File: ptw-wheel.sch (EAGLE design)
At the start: 5 parts

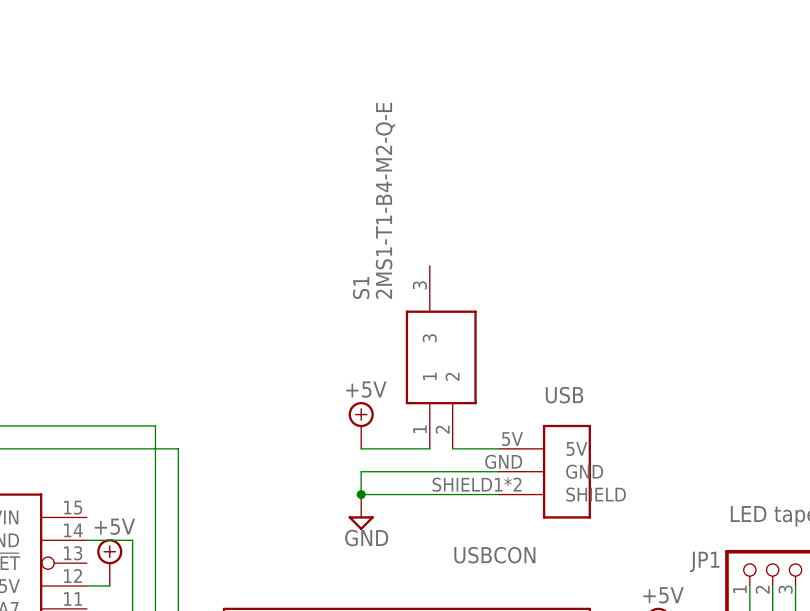
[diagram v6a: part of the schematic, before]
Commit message: - Replace toggle switch - Adjust positions
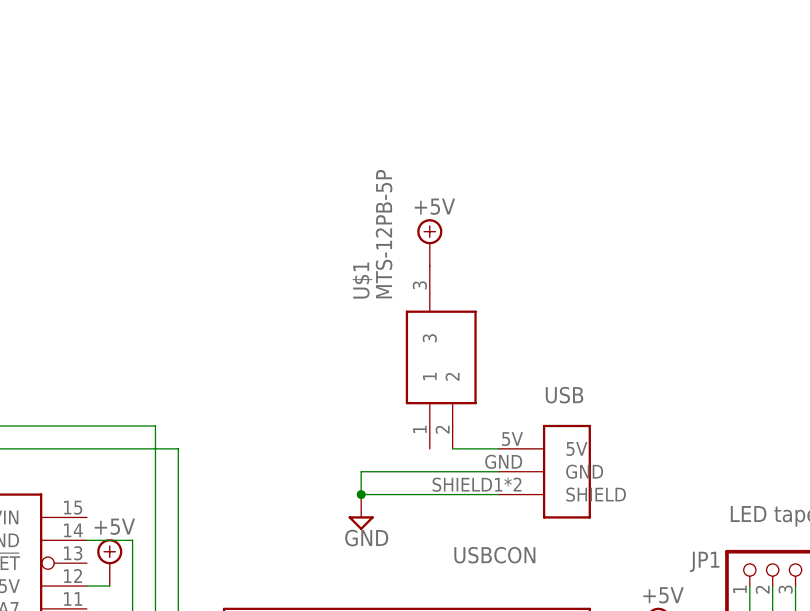
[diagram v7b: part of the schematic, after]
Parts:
- removed S1: 2MS1-T1-B4-M2-Q-E, 2MS1-T1-B4-VS2-Q-E:2MS1-T1-B4-M2-Q-E
- added U$1: MTS-12PB-5P, toggle-switch:MTS-12PB-5P
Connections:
- net +5V: now also U$1.3; no longer S1.1
- net N$1: now also U$1.2; no longer S1.2
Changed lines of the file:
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@@
 <part name="SUPPLY10" library="supply2" library_urn="urn:adsk.eagle:library:372" deviceset="GND" device=""/>
 <part name="KONASHI" library="konashiv2" deviceset="KONASHI2.0" device=""/>
-<part name="S1" library="2MS1-T1-B4-VS2-Q-E" deviceset="2MS1-T1-B4-M2-Q-E" device=""/>
+<part name="U$1" library="toggle-switch" deviceset="MTS-12PB-5P" device=""/>
 </parts>
 <sheets>
@@
 <attribute name="VALUE" x="51.435" y="34.925" size="1.778" layer="96"/>
 </instance>
-<instance part="SUPPLY6" gate="+5V" x="78.74" y="66.04" smashed="yes">
-<attribute name="VALUE" x="76.835" y="69.215" size="1.778" layer="96"/>
+<instance part="SUPPLY6" gate="+5V" x="86.36" y="86.36" smashed="yes">
+<attribute name="VALUE" x="84.455" y="89.535" size="1.778" layer="96"/>
 </instance>
 <instance part="SUPPLY9" gate="+5V" x="111.76" y="43.18" smashed="yes">
@@
 </instance>
 <instance part="KONASHI" gate="G$1" x="83.82" y="33.02" smashed="yes" rot="R90"/>
-<instance part="S1" gate="G$1" x="86.36" y="63.5" smashed="yes" rot="R90">
+<instance part="U$1" gate="G$1" x="86.36" y="63.5" smashed="yes" rot="R90">
 <attribute name="NAME" x="78.74" y="80.01" size="1.778" layer="95" rot="R90" align="center-left"/>
 <attribute name="VALUE" x="81.28" y="80.01" size="1.778" layer="96" rot="R90" align="center-left"/>
@@
 </segment>
 <segment>
-<pinref part="S1" gate="G$1" pin="1"/>
+<pinref part="U$1" gate="G$1" pin="3"/>
 <pinref part="SUPPLY6" gate="+5V" pin="+5V"/>
-<wire x1="78.74" y1="63.5" x2="86.36" y2="63.5" width="0.1524" layer="91"/>
 </segment>
 </net>
@@
 <segment>
 <pinref part="USB" gate="G$1" pin="5V"/>
-<pinref part="S1" gate="G$1" pin="2"/>
 <wire x1="93.98" y1="63.5" x2="88.9" y2="63.5" width="0.1524" layer="91"/>
+<pinref part="U$1" gate="G$1" pin="2"/>
 </segment>
 </net>
